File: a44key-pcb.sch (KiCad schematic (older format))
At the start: 64 parts, among them J1 AudioJack3, J2 Conn_01x04_Female, J3 Conn_01x04_Female, SW1 SW_Push, U1 ATmega32U4-AU, Y1 16MHz

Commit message: Rerouting
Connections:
- net GND: now also USB1.6 (SHIELD)
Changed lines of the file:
@@
 Connection ~ 1350 5250
 $Comp
-L power:GND #PWR?
+L power:GND #PWR0116
 U 1 1 61993731
 P 6350 6000
-F 0 "#PWR?" H 6350 5750 50  0001 C CNN
+F 0 "#PWR0116" H 6350 5750 50  0001 C CNN
 F 1 "GND" H 6355 5827 50  0000 C CNN
 F 2 "" H 6350 6000 50  0001 C CNN
@@
 $EndComp
 $Comp
-L power:GND #PWR?
+L power:GND #PWR0117
 U 1 1 61993FD0
 P 8150 5950
-F 0 "#PWR?" H 8150 5700 50  0001 C CNN
+F 0 "#PWR0117" H 8150 5700 50  0001 C CNN
 F 1 "GND" H 8155 5777 50  0000 C CNN
 F 2 "" H 8150 5950 50  0001 C CNN
@@
 Wire Wire Line
 	6350 5800 6350 6000
+Wire Wire Line
+	5500 1100 5750 1100
+Wire Wire Line
+	5750 1100 5750 1600
+Connection ~ 5750 1600
 $EndSCHEMATC

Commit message: Added the footprint libraries
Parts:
- added C11: 0.1uF, Capacitor_SMD:C_0805_2012Metric, symbol Device:C_Small
- added C9: 1uF, Capacitor_SMD:C_0805_2012Metric, symbol Device:C_Small
- added J4: Conn_01x04_Female, Connector_PinHeader_2.54mm:PinHeader_1x04_P2.54mm_Vertical, symbol Connector:Conn_01x04_Female
- added R5: 10k, Resistor_SMD:R_0805_2012Metric, symbol Device:R_Small
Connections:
- net +5V: now also F1.2, J1.3, USB1.5 (VBUS), C9.1; no longer C1.1, C4.1, C5.1, C8.1, F1.1, J1.2, R3.1, U1.14 (VCC), U1.24 (AVCC), U1.34 (VCC), U1.44 (AVCC)
- net GND: now also C11.1, C9.2, R5.1; no longer J2.1 (Pin_1), J2.4 (Pin_4), J3.1 (Pin_1), J3.4 (Pin_4), USB1.6 (SHIELD), Y1.2, Y1.4
- net SCL: now also J1.2; no longer J1.3
- net TH34: now also J4.3 (Pin_3)
- net TH35: now also J4.2 (Pin_2)
- net VCC: now also C1.1, C4.1, C5.1, C8.1, F1.1, R3.1, U1.14 (VCC), U1.24 (AVCC), U1.34 (VCC), U1.44 (AVCC); no longer F1.2, USB1.5 (VBUS)
- net at U1.12 (PB7): now also R5.2
- net at U1.42 (AREF): now also C11.2
- no-connect marks 0 -> 12
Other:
- moved on the sheet: J3

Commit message: {PCB
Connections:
- net COL4: now also MX8.2 (ROW); no longer MX8.1 (COL)
- net COL5: now also MX4.2 (ROW); no longer MX4.1 (COL)
- net TH34: now also MX8.1 (COL); no longer MX8.2 (ROW)
- net TH35: now also MX4.1 (COL); no longer MX4.2 (ROW)
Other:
- moved on the sheet: MX4, MX8
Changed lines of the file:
@@
 L MX_Alps_Hybrid:MX-NoLED MX4
 U 1 1 61713060
-P 6700 4750
-F 0 "MX4" H 6733 4973 60  0000 C CNN
-F 1 "MX-NoLED" H 6733 4899 20  0000 C CNN
-F 2 "MX_Alps_Hybrid:MX-Alps-Choc-X-1U-NoLED" H 6075 4725 60  0001 C CNN
-F 3 "" H 6075 4725 60  0001 C CNN
-	1    6700 4750
-	1    0    0    -1
+P 6750 4550
+F 0 "MX4" H 6783 4773 60  0000 C CNN
+F 1 "MX-NoLED" H 6783 4699 20  0000 C CNN
+F 2 "MX_Alps_Hybrid:MX-Alps-Choc-X-1U-NoLED" H 6125 4525 60  0001 C CNN
+F 3 "" H 6125 4525 60  0001 C CNN
+	1    6750 4550
+	-1   0    0    1
 $EndComp
 $Comp
@@
 $EndComp
 Wire Wire Line
-	6550 4900 6650 4900
+	6550 4900 6600 4900
 $Comp
 L MX_Alps_Hybrid:MX-NoLED MX8
 U 1 1 6171306D
-P 7400 4750
-F 0 "MX8" H 7433 4973 60  0000 C CNN
-F 1 "MX-NoLED" H 7433 4899 20  0000 C CNN
-F 2 "MX_Alps_Hybrid:MX-Alps-Choc-X-1U-NoLED" H 6775 4725 60  0001 C CNN
-F 3 "" H 6775 4725 60  0001 C CNN
-	1    7400 4750
-	1    0    0    -1
+P 7400 4600
+F 0 "MX8" H 7433 4823 60  0000 C CNN
+F 1 "MX-NoLED" H 7433 4749 20  0000 C CNN
+F 2 "MX_Alps_Hybrid:MX-Alps-Choc-X-1U-NoLED" H 6775 4575 60  0001 C CNN
+F 3 "" H 6775 4575 60  0001 C CNN
+	1    7400 4600
+	-1   0    0    1
 $EndComp
 $Comp
@@
 	0    -1   -1   0
 $EndComp
-Wire Wire Line
-	7250 4900 7350 4900
 $Comp
 L MX_Alps_Hybrid:MX-NoLED MX11
@@
 Connection ~ 6850 3100
 Wire Wire Line
-	6850 3900 6850 4700
-Connection ~ 6850 3900
-Wire Wire Line
 	7550 2300 7550 3100
 Wire Wire Line
 	7550 3100 7550 3900
 Connection ~ 7550 3100
-Wire Wire Line
-	7550 3900 7550 4700
-Connection ~ 7550 3900
 Wire Wire Line
 	8250 2300 8250 3100
@@
 Wire Wire Line
 	7250 4850 7250 4900
-Connection ~ 7250 4900
 $Comp
 L Device:C_Small C8
@@
 NoConn ~ 8100 6150
 NoConn ~ 8100 6450
+Wire Wire Line
+	6850 3900 6850 4400
+Wire Wire Line
+	6850 4400 6800 4400
+Connection ~ 6850 3900
+Wire Wire Line
+	6600 4600 6600 4900
+Wire Wire Line
+	7550 3900 7550 4450
+Wire Wire Line
+	7550 4450 7450 4450
+Connection ~ 7550 3900
+Wire Wire Line
+	7250 4650 7250 4850
+Connection ~ 7250 4850
 $EndSCHEMATC

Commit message: PCB
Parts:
- added Right-Left: JP1, Jumper:SolderJumper-3_P1.3mm_Open_Pad1.0x1.5mm, symbol Jumper:SolderJumper_3_Open
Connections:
- net GND: now also Right-Left.3 (B); no longer R4.1
- net VCC: now also Right-Left.1 (A)
- new net: R4.1, Right-Left.2 (C)
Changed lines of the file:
@@
 L power:GND #PWR0103
 U 1 1 616B6C85
-P 4900 4350
-F 0 "#PWR0103" H 4900 4100 50  0001 C CNN
-F 1 "GND" H 4905 4177 50  0000 C CNN
-F 2 "" H 4900 4350 50  0001 C CNN
-F 3 "" H 4900 4350 50  0001 C CNN
-	1    4900 4350
-	1    0    0    -1
-$EndComp
-Wire Wire Line
-	4900 4350 4650 4350
+P 4800 4550
+F 0 "#PWR0103" H 4800 4300 50  0001 C CNN
+F 1 "GND" H 4805 4377 50  0000 C CNN
+F 2 "" H 4800 4550 50  0001 C CNN
+F 3 "" H 4800 4550 50  0001 C CNN
+	1    4800 4550
+	1    0    0    -1
+$EndComp
 Connection ~ 4200 4350
 Wire Wire Line
@@
 	7250 4650 7250 4850
 Connection ~ 7250 4850
+$Comp
+L power:VCC #PWR0123
+U 1 1 61D90AAA
+P 4800 4150
+F 0 "#PWR0123" H 4800 4000 50  0001 C CNN
+F 1 "VCC" H 4817 4323 50  0000 C CNN
+F 2 "" H 4800 4150 50  0001 C CNN
+F 3 "" H 4800 4150 50  0001 C CNN
+	1    4800 4150
+	1    0    0    -1
+$EndComp
+$Comp
+L Jumper:SolderJumper_3_Open Right-Left
+U 1 1 61D817AC
+P 4800 4350
+F 0 "Right-Left" V 4754 4418 50  0000 L CNN
+F 1 "JP1" V 4845 4418 50  0000 L CNN
+F 2 "Jumper:SolderJumper-3_P1.3mm_Open_Pad1.0x1.5mm" H 4800 4350 50  0001 C CNN
+F 3 "~" H 4800 4350 50  0001 C CNN
+	1    4800 4350
+	0    1    1    0
+$EndComp
 $EndSCHEMATC

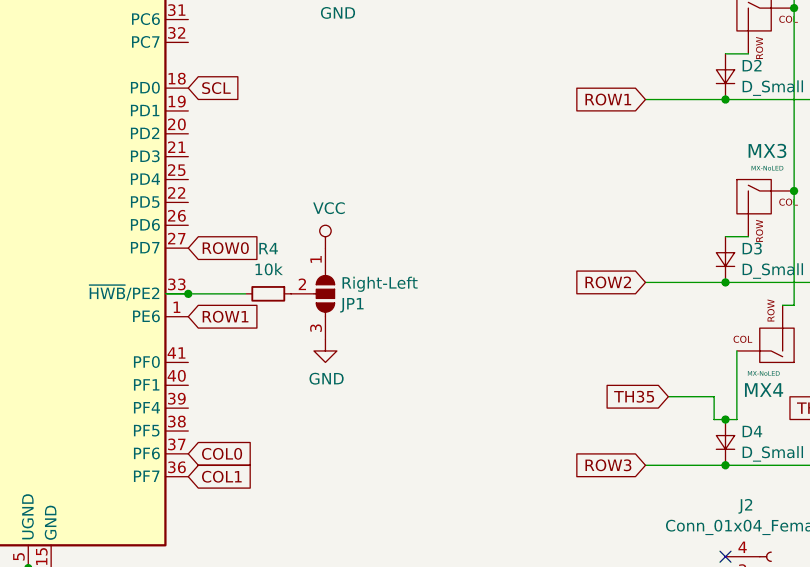
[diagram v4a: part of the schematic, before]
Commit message: PCB Left Hand Added
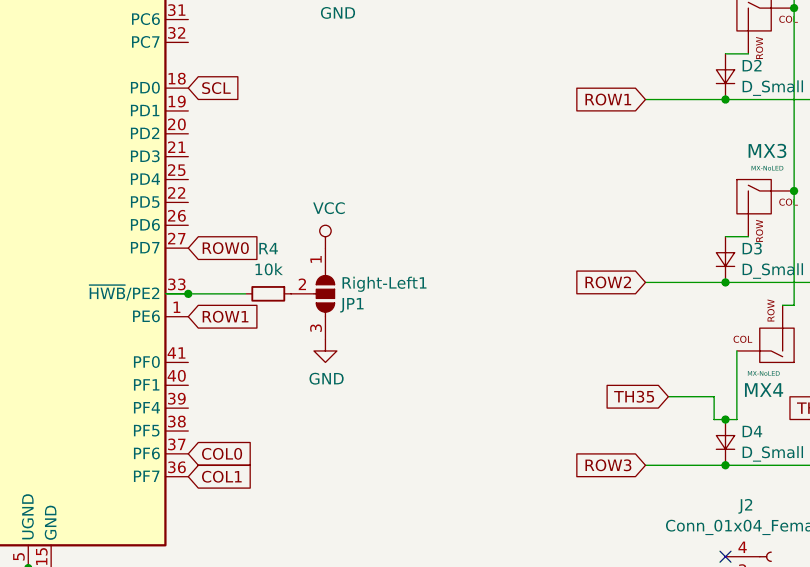
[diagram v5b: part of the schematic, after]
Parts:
- renumbered Right-Left to Right-Left1
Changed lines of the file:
@@
 $EndComp
 $Comp
-L Jumper:SolderJumper_3_Open Right-Left
+L Jumper:SolderJumper_3_Open Right-Left1
 U 1 1 61D817AC
 P 4800 4350
-F 0 "Right-Left" V 4754 4418 50  0000 L CNN
+F 0 "Right-Left1" V 4754 4418 50  0000 L CNN
 F 1 "JP1" V 4845 4418 50  0000 L CNN
 F 2 "Jumper:SolderJumper-3_P1.3mm_Open_Pad1.0x1.5mm" H 4800 4350 50  0001 C CNN

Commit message: Added parameters for the modifier to work nicelyDD
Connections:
- net GND: now also R4.1; no longer R5.1
- net at Right-Left1.2 (C): now also R5.1; no longer R4.1
- no-connect marks 12 -> 11
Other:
- moved on the sheet: Right-Left1
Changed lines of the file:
@@
 L power:GND #PWR0103
 U 1 1 616B6C85
-P 4800 4550
-F 0 "#PWR0103" H 4800 4300 50  0001 C CNN
-F 1 "GND" H 4805 4377 50  0000 C CNN
-F 2 "" H 4800 4550 50  0001 C CNN
-F 3 "" H 4800 4550 50  0001 C CNN
-	1    4800 4550
+P 4900 3150
+F 0 "#PWR0103" H 4900 2900 50  0001 C CNN
+F 1 "GND" H 4905 2977 50  0000 C CNN
+F 2 "" H 4900 3150 50  0001 C CNN
+F 3 "" H 4900 3150 50  0001 C CNN
+	1    4900 3150
 	1    0    0    -1
 $EndComp
@@
 L power:GND #PWR0116
 U 1 1 61DB9C67
-P 4850 2950
-F 0 "#PWR0116" H 4850 2700 50  0001 C CNN
-F 1 "GND" H 4855 2777 50  0000 C CNN
-F 2 "" H 4850 2950 50  0001 C CNN
-F 3 "" H 4850 2950 50  0001 C CNN
-	1    4850 2950
-	1    0    0    -1
-$EndComp
-Wire Wire Line
-	4750 2950 4850 2950
+P 4750 4350
+F 0 "#PWR0116" H 4750 4100 50  0001 C CNN
+F 1 "GND" H 4755 4177 50  0000 C CNN
+F 2 "" H 4750 4350 50  0001 C CNN
+F 3 "" H 4750 4350 50  0001 C CNN
+	1    4750 4350
+	1    0    0    -1
+$EndComp
+Wire Wire Line
+	4650 4350 4750 4350
 $Comp
 L power:+5V #PWR0115
@@
 NoConn ~ 5500 1500
 NoConn ~ 5500 1100
-NoConn ~ 5450 2550
 NoConn ~ 8050 5600
 NoConn ~ 8050 5900
@@
 L power:VCC #PWR0123
 U 1 1 61D90AAA
-P 4800 4150
-F 0 "#PWR0123" H 4800 4000 50  0001 C CNN
-F 1 "VCC" H 4817 4323 50  0000 C CNN
-F 2 "" H 4800 4150 50  0001 C CNN
-F 3 "" H 4800 4150 50  0001 C CNN
-	1    4800 4150
+P 4900 2750
+F 0 "#PWR0123" H 4900 2600 50  0001 C CNN
+F 1 "VCC" H 4917 2923 50  0000 C CNN
+F 2 "" H 4900 2750 50  0001 C CNN
+F 3 "" H 4900 2750 50  0001 C CNN
+	1    4900 2750
 	1    0    0    -1
 $EndComp
@@
 L Jumper:SolderJumper_3_Open Right-Left1
 U 1 1 61D817AC
-P 4800 4350
-F 0 "Right-Left1" V 4754 4418 50  0000 L CNN
-F 1 "JP1" V 4845 4418 50  0000 L CNN
-F 2 "Jumper:SolderJumper-3_P1.3mm_Open_Pad1.0x1.5mm" H 4800 4350 50  0001 C CNN
-F 3 "~" H 4800 4350 50  0001 C CNN
-	1    4800 4350
+P 4900 2950
+F 0 "Right-Left1" V 4854 3018 50  0000 L CNN
+F 1 "JP1" V 4945 3018 50  0000 L CNN
+F 2 "Jumper:SolderJumper-3_P1.3mm_Open_Pad1.0x1.5mm" H 4900 2950 50  0001 C CNN
+F 3 "~" H 4900 2950 50  0001 C CNN
+	1    4900 2950
 	0    1    1    0
 $EndComp
